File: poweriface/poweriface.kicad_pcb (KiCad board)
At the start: 2 copper layers, 25 x 42.5 mm, 20 parts, among them J1 Power Board, J2 CAN In, J3 CAN Out, J4 AVR-ISP-6, U1 ATmega32M1-AU, U2 MCP2551-I-SN, Y1 16MHz

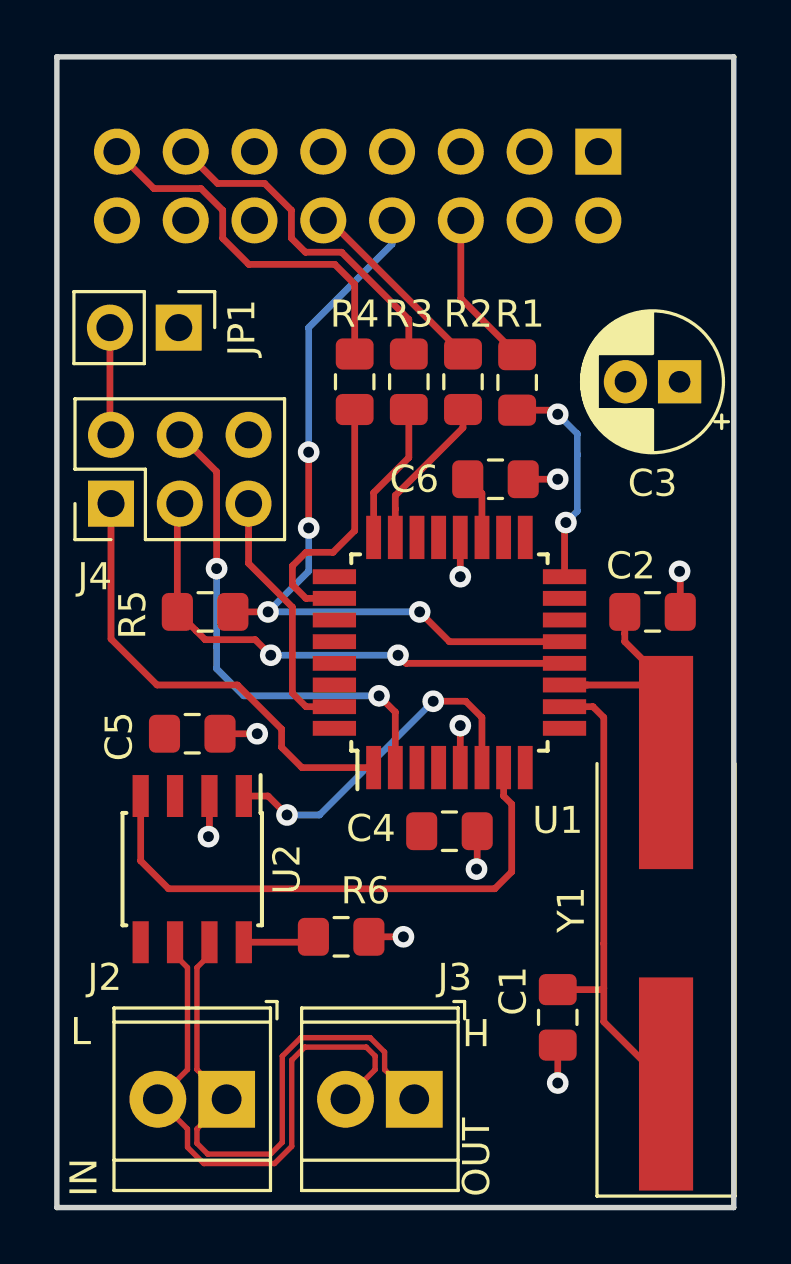
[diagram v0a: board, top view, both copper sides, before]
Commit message: Connected hispeed control to GPIO pin
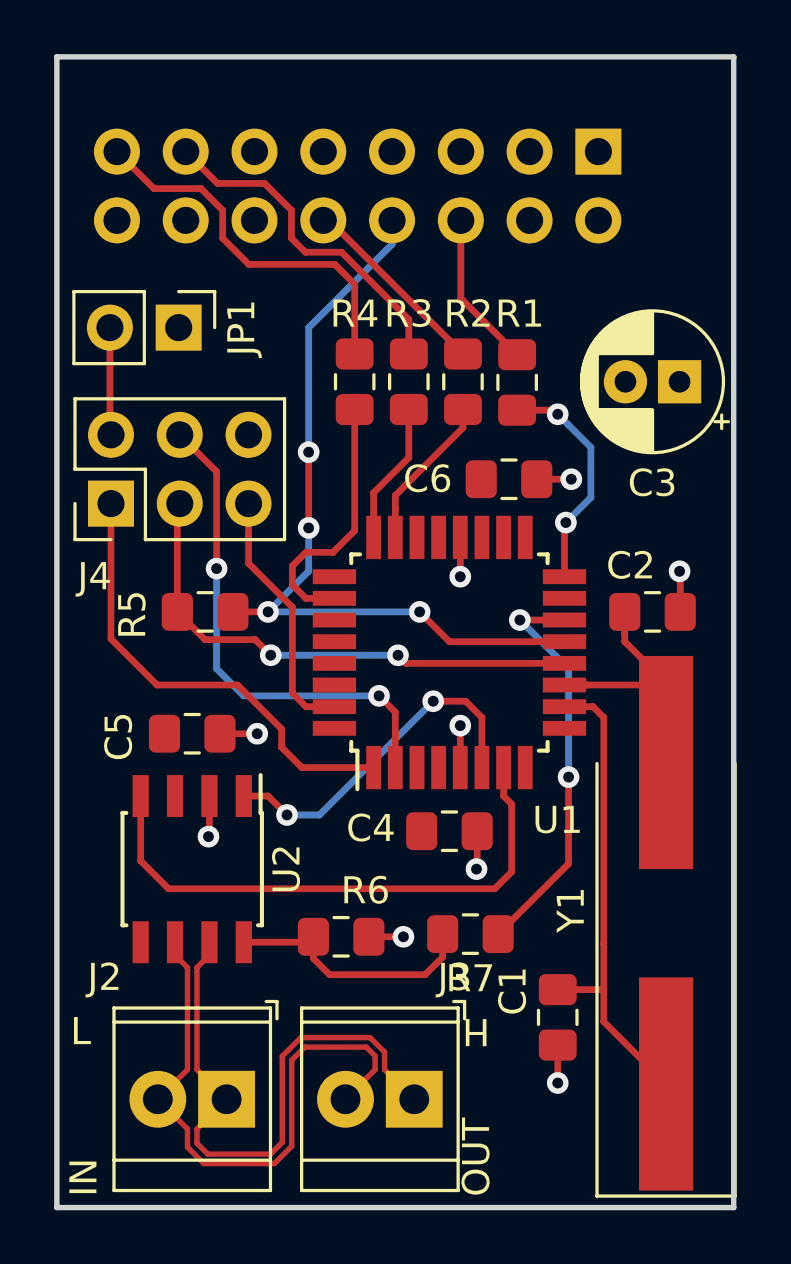
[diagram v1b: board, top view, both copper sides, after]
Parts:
- added R7: 0, Resistor_SMD:R_0805_2012Metric_Pad1.15x1.40mm_HandSolder, F.Cu at (185.3, 108.9)
- moved C6 0.50 mm to (186.7, 92.1)
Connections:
- U1 pad 14: (no net) -> /HISPEED
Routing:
- net /HISPEED: track 0.00 -> 15.1 mm, vias 0 -> 2
- net Net-(R6-Pad2): track 2.65 -> 9.60 mm
- net +5V: track 2.37 -> 0.00 mm
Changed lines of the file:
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@@
     (thickness 1.6)
     (drawings 10)
-    (tracks 181)
+    (tracks 191)
     (zones 0)
-    (modules 20)
-    (nets 24)
+    (modules 21)
+    (nets 25)
   )
   (page A4)
@@
   (net 22 /TXCAN)
   (net 23 /RXCAN)
+  (net 24 /HISPEED)
   (net_class Default "This is the default net class."
     (clearance 0.2)
@@
     (add_net /DIN)
     (add_net /DOUT)
+    (add_net /HISPEED)
     (add_net /MISOISP)
     (add_net /MOSIISP)
@@
     (pad 13 smd rect (at 0.4 4.25 180) (size 1.6 0.55) (layers F.Cu F.Paste F.Mask)
       (net 6 /ZCROSS))
-    (pad 14 smd rect (at 1.2 4.25 180) (size 1.6 0.55) (layers F.Cu F.Paste F.Mask))
+    (pad 14 smd rect (at 1.2 4.25 180) (size 1.6 0.55) (layers F.Cu F.Paste F.Mask)
+      (net 24 /HISPEED))
     (pad 15 smd rect (at 2 4.25 180) (size 1.6 0.55) (layers F.Cu F.Paste F.Mask))
     (pad 16 smd rect (at 2.8 4.25 180) (size 1.6 0.55) (layers F.Cu F.Paste F.Mask)
@@
   )
   (module Capacitor_SMD:C_0805_2012Metric_Pad1.15x1.40mm_HandSolder (layer F.Cu)
-    (at 186.2 92.1)
+    (at 186.7 92.1)
     (descr "Capacitor SMD 0805 (2012 Metric), square (rectangular) end terminal, IPC_7351 nominal with elongated pad for handsoldering. (Body size source: https://docs.google.com/spreadsheets/d/1BsfQQcO9C6DZCsRaXUlFlo91Tg2WpOkGARC1WS5S8t0/edit?usp=sharing), generated with kicad-footprint-generator")
     (tags "capacitor handsolder")
@@
       (net 1 GND))
     (model ${KISYS3DMOD}/Capacitor_SMD.3dshapes/C_0805_2012Metric.wrl
+      (at (xyz 0 0 0))
+      (scale (xyz 1 1 1))
+      (rotate (xyz 0 0 0))
+    )
+  )
+  (module Resistor_SMD:R_0805_2012Metric_Pad1.15x1.40mm_HandSolder (layer F.Cu)
+    (at 185.275 108.9 180)
+    (descr "Resistor SMD 0805 (2012 Metric), square (rectangular) end terminal, IPC_7351 nominal with elongated pad for handsoldering. (Body size source: https://docs.google.com/spreadsheets/d/1BsfQQcO9C6DZCsRaXUlFlo91Tg2WpOkGARC1WS5S8t0/edit?usp=sharing), generated with kicad-footprint-generator")
+    (tags "resistor handsolder")
+    (attr smd)
+    (fp_text reference R7 (at 0 -1.65 180) (layer F.SilkS)
+      (effects (font (size 1 1) (thickness 0.15)))
+    )
+    (fp_text value 0 (at 0 1.65 180) (layer F.Fab)
+      (effects (font (size 1 1) (thickness 0.15)))
+    )
+    (fp_line (start -1 0.6) (end -1 -0.6) (layer F.Fab) (width 0.1))
+    (fp_line (start -1 -0.6) (end 1 -0.6) (layer F.Fab) (width 0.1))
+    (fp_line (start 1 -0.6) (end 1 0.6) (layer F.Fab) (width 0.1))
+    (fp_line (start 1 0.6) (end -1 0.6) (layer F.Fab) (width 0.1))
+    (fp_line (start -0.261252 -0.71) (end 0.261252 -0.71) (layer F.SilkS) (width 0.12))
+    (fp_line (start -0.261252 0.71) (end 0.261252 0.71) (layer F.SilkS) (width 0.12))
+    (fp_line (start -1.85 0.95) (end -1.85 -0.95) (layer F.CrtYd) (width 0.05))
+    (fp_line (start -1.85 -0.95) (end 1.85 -0.95) (layer F.CrtYd) (width 0.05))
+    (fp_line (start 1.85 -0.95) (end 1.85 0.95) (layer F.CrtYd) (width 0.05))
+    (fp_line (start 1.85 0.95) (end -1.85 0.95) (layer F.CrtYd) (width 0.05))
+    (fp_text user %R (at 0 0 180) (layer F.Fab)
+      (effects (font (size 0.5 0.5) (thickness 0.08)))
+    )
+    (pad 1 smd roundrect (at -1.025 0 180) (size 1.15 1.4) (layers F.Cu F.Paste F.Mask) (roundrect_rratio 0.217391)
+      (net 24 /HISPEED))
+    (pad 2 smd roundrect (at 1.025 0 180) (size 1.15 1.4) (layers F.Cu F.Paste F.Mask) (roundrect_rratio 0.217391)
+      (net 21 "Net-(R6-Pad2)"))
+    (model ${KISYS3DMOD}/Resistor_SMD.3dshapes/R_0805_2012Metric.wrl
       (at (xyz 0 0 0))
       (scale (xyz 1 1 1))
@@
   (via (at 182.8 109) (size 0.8) (drill 0.4) (layers F.Cu B.Cu) (net 1))
   (segment (start 181.525 109) (end 182.8 109) (width 0.25) (layer F.Cu) (net 1))
-  (via (at 188.5 92.1) (size 0.8) (drill 0.4) (layers F.Cu B.Cu) (net 1))
-  (segment (start 187.225 92.1) (end 188.5 92.1) (width 0.25) (layer F.Cu) (net 1))
+  (via (at 189 92.1) (size 0.8) (drill 0.4) (layers F.Cu B.Cu) (net 1))
+  (segment (start 187.725 92.1) (end 189 92.1) (width 0.25) (layer F.Cu) (net 1))
   (segment (start 189.8 100.5) (end 190.2 100.9) (width 0.25) (layer F.Cu) (net 2))
   (segment (start 188.75 100.5) (end 189.8 100.5) (width 0.25) (layer F.Cu) (net 2))
@@
   (segment (start 192.5 100.8) (end 192.5 102.5625) (width 0.25) (layer F.Cu) (net 3))
   (segment (start 188.75 99.7) (end 192.5 99.7) (width 0.25) (layer F.Cu) (net 3))
-  (segment (start 185.7 92.625) (end 185.175 92.1) (width 0.25) (layer F.Cu) (net 4))
-  (segment (start 185.7 94.25) (end 185.7 92.625) (width 0.25) (layer F.Cu) (net 4))
   (segment (start 184.92 85.42) (end 185.6 86.1) (width 0.25) (layer F.Cu) (net 5))
   (segment (start 184.92 82.54) (end 184.92 85.42) (width 0.25) (layer F.Cu) (net 5))
@@
   (via (at 188.8 93.7) (size 0.8) (drill 0.4) (layers F.Cu B.Cu) (net 17))
   (segment (start 188.75 93.75) (end 188.8 93.7) (width 0.25) (layer F.Cu) (net 17))
-  (segment (start 188.8 93.7) (end 189.225001 93.274999) (width 0.25) (layer B.Cu) (net 17))
   (via (at 188.5 89.7) (size 0.8) (drill 0.4) (layers F.Cu B.Cu) (net 17))
   (segment (start 187 89.55) (end 188.35 89.55) (width 0.25) (layer F.Cu) (net 17))
   (segment (start 188.35 89.55) (end 188.5 89.7) (width 0.25) (layer F.Cu) (net 17))
-  (segment (start 189.225001 90.425001) (end 189.225001 91.2) (width 0.25) (layer B.Cu) (net 17))
-  (segment (start 188.5 89.7) (end 189.225001 90.425001) (width 0.25) (layer B.Cu) (net 17))
-  (segment (start 189.225001 93.274999) (end 189.225001 91.2) (width 0.25) (layer B.Cu) (net 17))
+  (segment (start 188.899999 90.099999) (end 188.5 89.7) (width 0.25) (layer B.Cu) (net 17))
+  (segment (start 189.725001 90.925001) (end 188.899999 90.099999) (width 0.25) (layer B.Cu) (net 17))
+  (segment (start 189.725001 92.774999) (end 189.725001 90.925001) (width 0.25) (layer B.Cu) (net 17))
+  (segment (start 188.8 93.7) (end 189.725001 92.774999) (width 0.25) (layer B.Cu) (net 17))
   (segment (start 182.5 93.2) (end 182.5 94.25) (width 0.25) (layer F.Cu) (net 18))
   (segment (start 182.5 92.7) (end 182.5 93.2) (width 0.25) (layer F.Cu) (net 18))
@@
   (segment (start 179.275 109.2) (end 179.475 109) (width 0.25) (layer F.Cu) (net 21))
   (segment (start 176.905 109.2) (end 179.275 109.2) (width 0.25) (layer F.Cu) (net 21))
+  (segment (start 179.475 109.8) (end 180.075 110.4) (width 0.25) (layer F.Cu) (net 21))
+  (segment (start 179.475 109) (end 179.475 109.8) (width 0.25) (layer F.Cu) (net 21))
+  (segment (start 180.075 110.4) (end 183.6 110.4) (width 0.25) (layer F.Cu) (net 21))
+  (segment (start 184.25 109.75) (end 184.25 108.9) (width 0.25) (layer F.Cu) (net 21))
+  (segment (start 183.6 110.4) (end 184.25 109.75) (width 0.25) (layer F.Cu) (net 21))
   (via (at 183.9 100.3) (size 0.8) (drill 0.4) (layers F.Cu B.Cu) (net 22))
   (segment (start 183.9 100.3) (end 185.1 100.3) (width 0.25) (layer F.Cu) (net 22))
@@
   (segment (start 186.174999 107.225001) (end 174.125001 107.225001) (width 0.25) (layer F.Cu) (net 23))
   (segment (start 186.8 106.6) (end 186.174999 107.225001) (width 0.25) (layer F.Cu) (net 23))
+  (via (at 188.9 103.1) (size 0.8) (drill 0.4) (layers F.Cu B.Cu) (net 24))
+  (segment (start 186.3 108.9) (end 188.9 106.3) (width 0.25) (layer F.Cu) (net 24))
+  (segment (start 188.9 106.3) (end 188.9 103.1) (width 0.25) (layer F.Cu) (net 24))
+  (segment (start 188.9 103.1) (end 188.9 99.1) (width 0.25) (layer B.Cu) (net 24))
+  (via (at 187.1 97.3) (size 0.8) (drill 0.4) (layers F.Cu B.Cu) (net 24))
+  (segment (start 188.9 99.1) (end 187.1 97.3) (width 0.25) (layer B.Cu) (net 24))
+  (segment (start 187.1 97.3) (end 188.75 97.3) (width 0.25) (layer F.Cu) (net 24))
   (zone (net 4) (net_name +5V) (layer F.Cu) (hatch edge 0.508)
     (connect_pads (clearance 0.25))

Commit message: Fixed small power plane issues
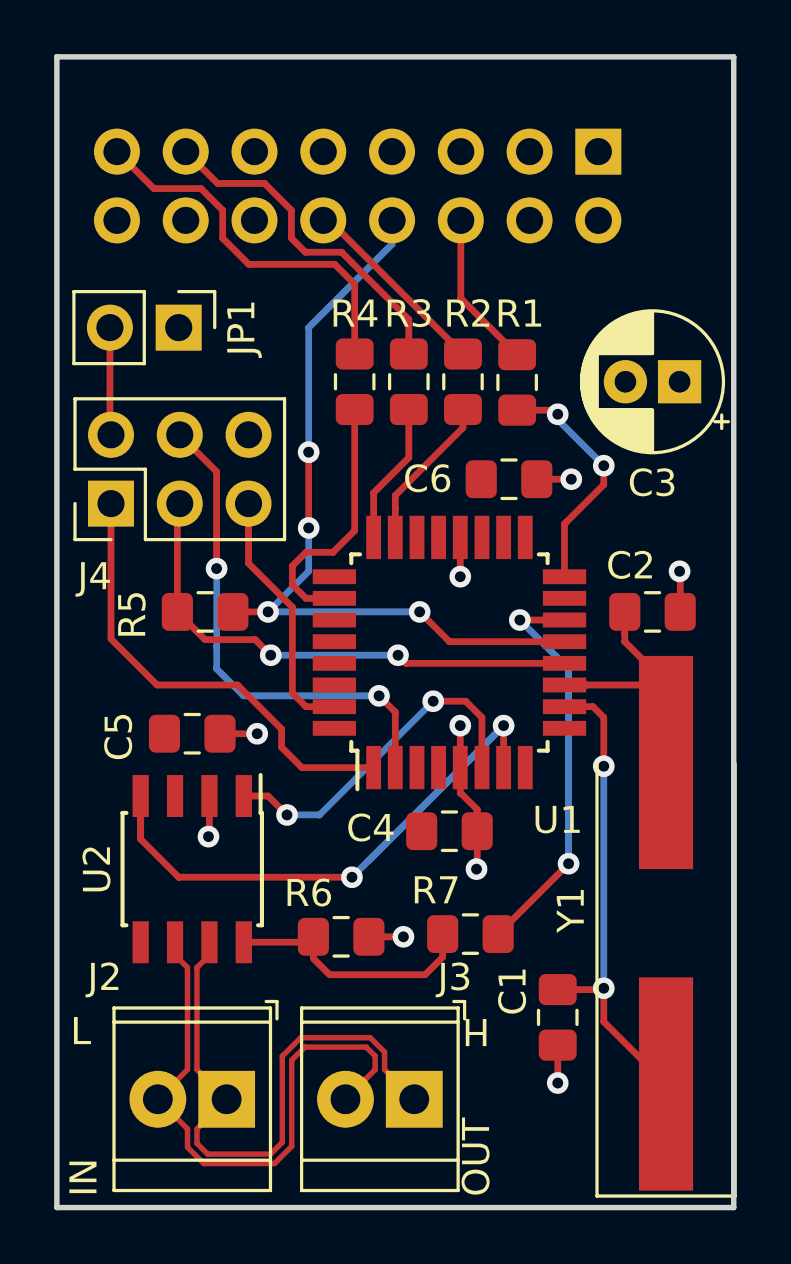
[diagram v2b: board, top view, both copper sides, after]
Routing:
- net /RXCAN: track 20.8 -> 28.0 mm, vias 0 -> 2
- net GND: track 12.8 -> 15.4 mm
- net Net-(C1-Pad2): vias 0 -> 2
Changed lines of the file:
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@@
     (thickness 1.6)
     (drawings 10)
-    (tracks 191)
+    (tracks 199)
     (zones 0)
     (modules 21)
@@
     (tags "resistor handsolder")
     (attr smd)
-    (fp_text reference R6 (at -0.9 1.7 180) (layer F.SilkS)
+    (fp_text reference R6 (at 1.2 1.6 180) (layer F.SilkS)
       (effects (font (size 1 1) (thickness 0.15)))
     )
@@
     (tags "SOIC 1.27")
     (attr smd)
-    (fp_text reference U2 (at 0 -3.5 270) (layer F.SilkS)
+    (fp_text reference U2 (at 0 3.5 270) (layer F.SilkS)
       (effects (font (size 1 1) (thickness 0.15)))
     )
@@
     (tags "resistor handsolder")
     (attr smd)
-    (fp_text reference R7 (at 0 -1.65 180) (layer F.SilkS)
+    (fp_text reference R7 (at 1.275 1.6 180) (layer F.SilkS)
       (effects (font (size 1 1) (thickness 0.15)))
     )
@@
   (via (at 189 92.1) (size 0.8) (drill 0.4) (layers F.Cu B.Cu) (net 1))
   (segment (start 187.725 92.1) (end 189 92.1) (width 0.25) (layer F.Cu) (net 1))
+  (segment (start 184.925 103.7) (end 184.9 103.7) (width 0.25) (layer F.Cu) (net 1))
+  (segment (start 185.525 105.1) (end 185.525 104.3) (width 0.25) (layer F.Cu) (net 1))
+  (segment (start 185.525 104.3) (end 184.925 103.7) (width 0.25) (layer F.Cu) (net 1))
+  (segment (start 184.9 103.7) (end 184.9 102.75) (width 0.25) (layer F.Cu) (net 1))
   (segment (start 189.8 100.5) (end 190.2 100.9) (width 0.25) (layer F.Cu) (net 2))
   (segment (start 188.75 100.5) (end 189.8 100.5) (width 0.25) (layer F.Cu) (net 2))
-  (segment (start 190.2 100.9) (end 190.2 109.25) (width 0.25) (layer F.Cu) (net 2))
   (segment (start 190.2 112.1375) (end 192.5 114.4375) (width 0.25) (layer F.Cu) (net 2))
   (segment (start 190.15 110.95) (end 190.2 110.9) (width 0.25) (layer F.Cu) (net 2))
   (segment (start 188.5 110.95) (end 190.15 110.95) (width 0.25) (layer F.Cu) (net 2))
-  (segment (start 190.2 109.25) (end 190.2 110.9) (width 0.25) (layer F.Cu) (net 2))
   (segment (start 190.2 110.9) (end 190.2 112.1375) (width 0.25) (layer F.Cu) (net 2))
+  (via (at 190.2 110.9) (size 0.8) (drill 0.4) (layers F.Cu B.Cu) (net 2))
+  (segment (start 190.2 110.9) (end 190.2 102.7) (width 0.25) (layer B.Cu) (net 2))
+  (segment (start 190.2 100.9) (end 190.2 102.7) (width 0.25) (layer F.Cu) (net 2))
+  (via (at 190.2 102.7) (size 0.8) (drill 0.4) (layers F.Cu B.Cu) (net 2))
   (segment (start 190.975 98.1) (end 190.975 97.8) (width 0.25) (layer F.Cu) (net 3))
   (segment (start 192.5 99.625) (end 190.975 98.1) (width 0.25) (layer F.Cu) (net 3))
@@
   (segment (start 178.7 100) (end 178.7 96.826998) (width 0.25) (layer F.Cu) (net 16))
   (segment (start 188.75 95.7) (end 188.75 93.75) (width 0.25) (layer F.Cu) (net 17))
-  (via (at 188.8 93.7) (size 0.8) (drill 0.4) (layers F.Cu B.Cu) (net 17))
   (segment (start 188.75 93.75) (end 188.8 93.7) (width 0.25) (layer F.Cu) (net 17))
   (via (at 188.5 89.7) (size 0.8) (drill 0.4) (layers F.Cu B.Cu) (net 17))
   (segment (start 187 89.55) (end 188.35 89.55) (width 0.25) (layer F.Cu) (net 17))
   (segment (start 188.35 89.55) (end 188.5 89.7) (width 0.25) (layer F.Cu) (net 17))
-  (segment (start 188.899999 90.099999) (end 188.5 89.7) (width 0.25) (layer B.Cu) (net 17))
-  (segment (start 189.725001 90.925001) (end 188.899999 90.099999) (width 0.25) (layer B.Cu) (net 17))
-  (segment (start 189.725001 92.774999) (end 189.725001 90.925001) (width 0.25) (layer B.Cu) (net 17))
-  (segment (start 188.8 93.7) (end 189.725001 92.774999) (width 0.25) (layer B.Cu) (net 17))
+  (via (at 190.2 91.6) (size 0.8) (drill 0.4) (layers F.Cu B.Cu) (net 17))
+  (segment (start 188.8 93.7) (end 190.2 92.3) (width 0.25) (layer F.Cu) (net 17))
+  (segment (start 190.2 92.3) (end 190.2 91.6) (width 0.25) (layer F.Cu) (net 17))
+  (segment (start 188.5 89.9) (end 188.5 89.7) (width 0.25) (layer B.Cu) (net 17))
+  (segment (start 190.2 91.6) (end 188.5 89.9) (width 0.25) (layer B.Cu) (net 17))
   (segment (start 182.5 93.2) (end 182.5 94.25) (width 0.25) (layer F.Cu) (net 18))
   (segment (start 182.5 92.7) (end 182.5 93.2) (width 0.25) (layer F.Cu) (net 18))
@@
   (segment (start 179.7 104.5) (end 183.9 100.3) (width 0.25) (layer B.Cu) (net 22))
   (segment (start 178.5 104.5) (end 179.7 104.5) (width 0.25) (layer B.Cu) (net 22))
-  (segment (start 186.5 103.8) (end 186.8 104.1) (width 0.25) (layer F.Cu) (net 23))
-  (segment (start 186.5 102.75) (end 186.5 103.8) (width 0.25) (layer F.Cu) (net 23))
-  (segment (start 186.8 104.1) (end 186.8 106.6) (width 0.25) (layer F.Cu) (net 23))
-  (segment (start 173.095 106.195) (end 173.095 103.8) (width 0.25) (layer F.Cu) (net 23))
-  (segment (start 174.125001 107.225001) (end 173.095 106.195) (width 0.25) (layer F.Cu) (net 23))
-  (segment (start 186.174999 107.225001) (end 174.125001 107.225001) (width 0.25) (layer F.Cu) (net 23))
-  (segment (start 186.8 106.6) (end 186.174999 107.225001) (width 0.25) (layer F.Cu) (net 23))
-  (via (at 188.9 103.1) (size 0.8) (drill 0.4) (layers F.Cu B.Cu) (net 24))
+  (segment (start 173.095 103.8) (end 173.095 105.295) (width 0.25) (layer F.Cu) (net 23))
+  (segment (start 186.5 101.2) (end 181.5 106.2) (width 0.25) (layer B.Cu) (net 23))
+  (via (at 186.5 101.2) (size 0.8) (drill 0.4) (layers F.Cu B.Cu) (net 23))
+  (segment (start 186.5 102.75) (end 186.5 101.2) (width 0.25) (layer F.Cu) (net 23))
+  (segment (start 173.095 103.8) (end 173.095 105.395) (width 0.25) (layer F.Cu) (net 23))
+  (via (at 180.9 106.8) (size 0.8) (drill 0.4) (layers F.Cu B.Cu) (net 23))
+  (segment (start 173.095 105.395) (end 174.5 106.8) (width 0.25) (layer F.Cu) (net 23))
+  (segment (start 174.5 106.8) (end 180.9 106.8) (width 0.25) (layer F.Cu) (net 23))
+  (segment (start 180.9 106.8) (end 186.5 101.2) (width 0.25) (layer B.Cu) (net 23))
   (segment (start 186.3 108.9) (end 188.9 106.3) (width 0.25) (layer F.Cu) (net 24))
-  (segment (start 188.9 106.3) (end 188.9 103.1) (width 0.25) (layer F.Cu) (net 24))
   (segment (start 188.9 103.1) (end 188.9 99.1) (width 0.25) (layer B.Cu) (net 24))
   (via (at 187.1 97.3) (size 0.8) (drill 0.4) (layers F.Cu B.Cu) (net 24))
   (segment (start 188.9 99.1) (end 187.1 97.3) (width 0.25) (layer B.Cu) (net 24))
   (segment (start 187.1 97.3) (end 188.75 97.3) (width 0.25) (layer F.Cu) (net 24))
+  (via (at 188.9 106.3) (size 0.8) (drill 0.4) (layers F.Cu B.Cu) (net 24))
+  (segment (start 188.9 103.1) (end 188.9 106.3) (width 0.25) (layer B.Cu) (net 24))
   (zone (net 4) (net_name +5V) (layer F.Cu) (hatch edge 0.508)
     (connect_pads (clearance 0.25))
